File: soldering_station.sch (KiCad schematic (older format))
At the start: 21 parts

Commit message: Change atmega48 to atmega8a
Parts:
- removed U?: ATMEGA48A-PU, DIL28, symbol ATMEGA48A-PU
- added IC?: ATMEGA8A-P, DIL28, symbol ATMEGA8A-P
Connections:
- wire segments 49 -> 61
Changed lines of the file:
@@
 	1    0    0    -1
 $EndComp
-$Comp
-L ATMEGA48A-PU U?
-U 0 1 5901F504
-P 5300 3200
-F 0 "U?" H 5350 4567 50  0000 C CNN
-F 1 "ATMEGA48A-PU" H 5350 4476 50  0000 C CNN
-F 2 "DIL28" H 5300 3200 50  0001 C CIN
-F 3 "" H 5300 3200 50  0001 C CNN
-	0    5300 3200
-	1    0    0    -1
-$EndComp
-Wire Wire Line
-	7150 3900 6300 3900
-Wire Wire Line
-	7150 2200 7150 3900
+Wire Wire Line
+	7150 3850 6300 3850
+Wire Wire Line
+	7150 2200 7150 3850
 Wire Wire Line
 	9850 2200 7150 2200
@@
 Connection ~ 8150 1350
 Wire Wire Line
-	6900 1350 7800 1350
+	6900 1350 7750 1350
+Wire Wire Line
+	7750 1350 7800 1350
 Wire Wire Line
 	7750 1550 7750 1350
@@
 	7750 1750 7750 1850
 Wire Wire Line
-	8100 1350 8250 1350
+	8100 1350 8150 1350
+Wire Wire Line
+	8150 1350 8250 1350
 Wire Wire Line
 	8150 850  8150 1350
@@
 	8350 700  8350 650
 Wire Wire Line
-	8500 850  9100 850
+	8500 850  8550 850
+Wire Wire Line
+	8550 850  9100 850
 Wire Wire Line
 	8550 650  8550 850
 Wire Wire Line
-	9100 1200 9100 1500
+	9100 1200 9100 1450
+Wire Wire Line
+	9100 1450 9100 1500
 Wire Wire Line
 	9100 1800 9100 1850
@@
 Connection ~ 9600 1250
 Wire Wire Line
-	9600 1200 9600 1550
+	9600 1200 9600 1250
+Wire Wire Line
+	9600 1250 9600 1550
 Wire Wire Line
 	9600 1850 9600 1750
 Wire Wire Line
-	9550 1250 10450 1250
+	9550 1250 9600 1250
+Wire Wire Line
+	9600 1250 10450 1250
 $Comp
 L GND #PWR?
@@
 Connection ~ 8150 3050
 Wire Wire Line
-	6300 3050 7800 3050
+	6300 3050 7750 3050
+Wire Wire Line
+	7750 3050 7800 3050
 Wire Wire Line
 	7750 3250 7750 3050
@@
 	7750 3450 7750 3550
 Wire Wire Line
-	8100 3050 8250 3050
+	8100 3050 8150 3050
+Wire Wire Line
+	8150 3050 8250 3050
 Wire Wire Line
 	8150 2550 8150 3050
@@
 	8350 2400 8350 2350
 Wire Wire Line
-	8500 2550 9100 2550
+	8500 2550 8550 2550
+Wire Wire Line
+	8550 2550 9100 2550
 Wire Wire Line
 	8550 2350 8550 2550
 Wire Wire Line
-	9100 2900 9100 3200
+	9100 2900 9100 3150
+Wire Wire Line
+	9100 3150 9100 3200
 Wire Wire Line
 	9100 3500 9100 3550
@@
 Connection ~ 9600 2950
 Wire Wire Line
-	9600 2900 9600 3250
+	9600 2900 9600 2950
+Wire Wire Line
+	9600 2950 9600 3250
 Wire Wire Line
 	9600 3550 9600 3450
 Wire Wire Line
-	9550 2950 10450 2950
+	9550 2950 9600 2950
+Wire Wire Line
+	9600 2950 10450 2950
 $Comp
 L CONN_01X05 J?
@@
 	1    0    0    -1
 $EndComp
+$Comp
+L ATMEGA8A-P IC?
+U 1 1 5912C25D
+P 5300 3350
+F 0 "IC?" H 5350 5018 50  0000 C CNN
+F 1 "ATMEGA8A-P" H 5350 4927 50  0000 C CNN
+F 2 "DIL28" H 5350 4836 50  0000 C CIN
+F 3 "" H 5300 3350 50  0000 C CNN
+	1    5300 3350
+	1    0    0    -1
+$EndComp

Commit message: Add encoder
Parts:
- added BZ?: Buzzer, symbol Buzzer
- added R?: R, symbol R
- added SW?: Rotary_Encoder, symbol Rotary_Encoder
- J?: value CONN_01X05 -> soldering iron
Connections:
- wire segments 61 -> 64
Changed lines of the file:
@@
 U 1 1 5901D04C
 P 8550 1350
-F 0 "U?" H 8600 1050 50  0000 L CNN
-F 1 "TL072" H 8550 1150 50  0000 L CNN
+F 0 "U?" H 8650 1650 50  0000 L CNN
+F 1 "TL072" H 8600 1550 50  0000 L CNN
 F 2 "" H 8550 1350 50  0001 C CNN
 F 3 "" H 8550 1350 50  0001 C CNN
@@
 U 2 1 5901D0A9
 P 8550 3050
-F 0 "U?" H 8891 3096 50  0000 L CNN
-F 1 "TL072" H 8891 3005 50  0000 L CNN
+F 0 "U?" H 8650 3350 50  0000 L CNN
+F 1 "TL072" H 8600 3250 50  0000 L CNN
 F 2 "" H 8550 3050 50  0001 C CNN
 F 3 "" H 8550 3050 50  0001 C CNN
@@
 U 0 1 5901D157
 P 10650 1600
-F 0 "J?" H 10569 1025 50  0000 C CNN
-F 1 "CONN_01X08" H 10569 1116 50  0000 C CNN
+F 0 "J?" H 10600 2200 50  0000 C CNN
+F 1 "CONN_01X08" H 10700 2100 50  0000 C CNN
 F 2 "" H 10650 1600 50  0001 C CNN
 F 3 "" H 10650 1600 50  0001 C CNN
@@
 P 9600 1850
 F 0 "#PWR?" H 9600 1600 50  0001 C CNN
-F 1 "GND" H 9605 1677 50  0000 C CNN
+F 1 "GND" H 9750 1800 50  0000 C CNN
 F 2 "" H 9600 1850 50  0001 C CNN
 F 3 "" H 9600 1850 50  0001 C CNN
@@
 P 9600 750
 F 0 "#PWR?" H 9600 600 50  0001 C CNN
-F 1 "+5V" H 9615 923 50  0000 C CNN
+F 1 "+5V" H 9750 850 50  0000 C CNN
 F 2 "" H 9600 750 50  0001 C CNN
 F 3 "" H 9600 750 50  0001 C CNN
@@
 P 9100 1850
 F 0 "#PWR?" H 9100 1600 50  0001 C CNN
-F 1 "GND" H 9105 1677 50  0000 C CNN
+F 1 "GND" H 9250 1800 50  0000 C CNN
 F 2 "" H 9100 1850 50  0001 C CNN
 F 3 "" H 9100 1850 50  0001 C CNN
@@
 P 7750 1850
 F 0 "#PWR?" H 7750 1600 50  0001 C CNN
-F 1 "GND" H 7755 1677 50  0000 C CNN
+F 1 "GND" H 7900 1800 50  0000 C CNN
 F 2 "" H 7750 1850 50  0001 C CNN
 F 3 "" H 7750 1850 50  0001 C CNN
@@
 P 8650 750
 F 0 "#PWR?" H 8650 600 50  0001 C CNN
-F 1 "+5V" H 8665 923 50  0000 C CNN
+F 1 "+5V" H 8800 850 50  0000 C CNN
 F 2 "" H 8650 750 50  0001 C CNN
 F 3 "" H 8650 750 50  0001 C CNN
@@
 P 8650 1850
 F 0 "#PWR?" H 8650 1600 50  0001 C CNN
-F 1 "GND" H 8655 1677 50  0000 C CNN
+F 1 "GND" H 8800 1800 50  0000 C CNN
 F 2 "" H 8650 1850 50  0001 C CNN
 F 3 "" H 8650 1850 50  0001 C CNN
@@
 $EndComp
 Wire Wire Line
-	7150 3850 6300 3850
-Wire Wire Line
-	7150 2200 7150 3850
-Wire Wire Line
-	9850 2200 7150 2200
+	7200 2200 7200 3150
+Wire Wire Line
+	9850 2200 7200 2200
 Wire Wire Line
 	9850 1350 9850 2200
@@
 Connection ~ 8150 1350
 Wire Wire Line
-	6900 1350 7750 1350
-Wire Wire Line
-	7750 1350 7800 1350
+	6900 1350 7800 1350
 Wire Wire Line
 	7750 1550 7750 1350
@@
 	7750 1750 7750 1850
 Wire Wire Line
-	8100 1350 8150 1350
-Wire Wire Line
-	8150 1350 8250 1350
+	8100 1350 8250 1350
 Wire Wire Line
 	8150 850  8150 1350
@@
 	8350 700  8350 650
 Wire Wire Line
-	8500 850  8550 850
-Wire Wire Line
-	8550 850  9100 850
+	8500 850  9100 850
 Wire Wire Line
 	8550 650  8550 850
 Wire Wire Line
-	9100 1200 9100 1450
-Wire Wire Line
-	9100 1450 9100 1500
+	9100 1200 9100 1500
 Wire Wire Line
 	9100 1800 9100 1850
@@
 Connection ~ 9600 1250
 Wire Wire Line
-	9600 1200 9600 1250
-Wire Wire Line
-	9600 1250 9600 1550
+	9600 1200 9600 1550
 Wire Wire Line
 	9600 1850 9600 1750
 Wire Wire Line
-	9550 1250 9600 1250
-Wire Wire Line
-	9600 1250 10450 1250
+	9550 1250 10450 1250
 $Comp
 L GND #PWR?
@@
 P 9600 3550
 F 0 "#PWR?" H 9600 3300 50  0001 C CNN
-F 1 "GND" H 9605 3377 50  0000 C CNN
+F 1 "GND" H 9750 3500 50  0000 C CNN
 F 2 "" H 9600 3550 50  0001 C CNN
 F 3 "" H 9600 3550 50  0001 C CNN
@@
 P 9600 2450
 F 0 "#PWR?" H 9600 2300 50  0001 C CNN
-F 1 "+5V" H 9615 2623 50  0000 C CNN
+F 1 "+5V" H 9750 2550 50  0000 C CNN
 F 2 "" H 9600 2450 50  0001 C CNN
 F 3 "" H 9600 2450 50  0001 C CNN
@@
 P 9100 3550
 F 0 "#PWR?" H 9100 3300 50  0001 C CNN
-F 1 "GND" H 9105 3377 50  0000 C CNN
+F 1 "GND" H 9250 3500 50  0000 C CNN
 F 2 "" H 9100 3550 50  0001 C CNN
 F 3 "" H 9100 3550 50  0001 C CNN
@@
 P 8650 2450
 F 0 "#PWR?" H 8650 2300 50  0001 C CNN
-F 1 "+5V" H 8665 2623 50  0000 C CNN
+F 1 "+5V" H 8800 2550 50  0000 C CNN
 F 2 "" H 8650 2450 50  0001 C CNN
 F 3 "" H 8650 2450 50  0001 C CNN
@@
 P 8650 3550
 F 0 "#PWR?" H 8650 3300 50  0001 C CNN
-F 1 "GND" H 8655 3377 50  0000 C CNN
+F 1 "GND" H 8800 3500 50  0000 C CNN
 F 2 "" H 8650 3550 50  0001 C CNN
 F 3 "" H 8650 3550 50  0001 C CNN
@@
 Connection ~ 8150 3050
 Wire Wire Line
-	6300 3050 7750 3050
-Wire Wire Line
-	7750 3050 7800 3050
+	6300 3050 7800 3050
 Wire Wire Line
 	7750 3250 7750 3050
@@
 	7750 3450 7750 3550
 Wire Wire Line
-	8100 3050 8150 3050
-Wire Wire Line
-	8150 3050 8250 3050
+	8100 3050 8250 3050
 Wire Wire Line
 	8150 2550 8150 3050
@@
 	8350 2400 8350 2350
 Wire Wire Line
-	8500 2550 8550 2550
-Wire Wire Line
-	8550 2550 9100 2550
+	8500 2550 9100 2550
 Wire Wire Line
 	8550 2350 8550 2550
 Wire Wire Line
-	9100 2900 9100 3150
-Wire Wire Line
-	9100 3150 9100 3200
+	9100 2900 9100 3200
 Wire Wire Line
 	9100 3500 9100 3550
@@
 Connection ~ 9600 2950
 Wire Wire Line
-	9600 2900 9600 2950
-Wire Wire Line
-	9600 2950 9600 3250
+	9600 2900 9600 3250
 Wire Wire Line
 	9600 3550 9600 3450
 Wire Wire Line
-	9550 2950 9600 2950
-Wire Wire Line
-	9600 2950 10450 2950
+	9550 2950 10450 2950
 $Comp
 L CONN_01X05 J?
 U 0 1 59021679
 P 10650 3150
-F 0 "J?" H 10728 3191 50  0000 L CNN
-F 1 "CONN_01X05" H 10728 3100 50  0000 L CNN
+F 0 "J?" H 10550 3600 50  0000 L CNN
+F 1 "soldering iron" H 10500 3500 50  0000 L CNN
 F 2 "" H 10650 3150 50  0001 C CNN
 F 3 "" H 10650 3150 50  0001 C CNN
@@
 	1    0    0    -1
 $EndComp
+$Comp
+L GND #PWR?
+U 1 1 5912E7A7
+P 10000 1500
+F 0 "#PWR?" H 10000 1250 50  0001 C CNN
+F 1 "GND" H 10005 1327 50  0000 C CNN
+F 2 "" H 10000 1500 50  0000 C CNN
+F 3 "" H 10000 1500 50  0000 C CNN
+	1    10000 1500
+	1    0    0    -1
+$EndComp
+Wire Wire Line
+	10450 1450 10000 1450
+Wire Wire Line
+	10000 1450 10000 1500
+$Comp
+L Buzzer BZ?
+U 1 1 5913130E
+P 6800 4450
+F 0 "BZ?" H 6953 4479 50  0000 L CNN
+F 1 "Buzzer" H 6953 4388 50  0000 L CNN
+F 2 "" V 6775 4550 50  0000 C CNN
+F 3 "" V 6775 4550 50  0000 C CNN
+	1    6800 4450
+	1    0    0    -1
+$EndComp
+Wire Wire Line
+	7200 3150 6300 3150
+$Comp
+L GND #PWR?
+U 1 1 59131E18
+P 6400 4650
+F 0 "#PWR?" H 6400 4400 50  0001 C CNN
+F 1 "GND" H 6405 4477 50  0000 C CNN
+F 2 "" H 6400 4650 50  0000 C CNN
+F 3 "" H 6400 4650 50  0000 C CNN
+	1    6400 4650
+	1    0    0    -1
+$EndComp
+Wire Wire Line
+	6700 4550 6400 4550
+Wire Wire Line
+	6400 4550 6400 4650
+$Comp
+L R R?
+U 1 1 59131FE4
+P 6500 4350
+F 0 "R?" V 6293 4350 50  0000 C CNN
+F 1 "R" V 6384 4350 50  0000 C CNN
+F 2 "" V 6430 4350 50  0000 C CNN
+F 3 "" H 6500 4350 50  0000 C CNN
+	1    6500 4350
+	0    1    1    0
+$EndComp
+Wire Wire Line
+	6650 4350 6700 4350
+Wire Wire Line
+	6350 4350 6300 4350
+$Comp
+L Rotary_Encoder SW?
+U 1 1 59133B57
+P 7000 3450
+F 0 "SW?" H 7229 3496 50  0000 L CNN
+F 1 "Rotary_Encoder" H 7229 3405 50  0000 L CNN
+F 2 "" H 6900 3610 50  0001 C CNN
+F 3 "" H 7000 3710 50  0001 C CNN
+	1    7000 3450
+	1    0    0    -1
+$EndComp
+Wire Wire Line
+	6300 3250 6600 3250
+Wire Wire Line
+	6600 3250 6600 3350
+Wire Wire Line
+	6600 3350 6700 3350
+Wire Wire Line
+	6700 3450 6500 3450
+Wire Wire Line
+	6500 3450 6500 3350
+Wire Wire Line
+	6500 3350 6300 3350
+Wire Wire Line
+	6300 3450 6400 3450
+Wire Wire Line
+	6400 3450 6400 3550
+Wire Wire Line
+	6400 3550 6700 3550
 $EndSCHEMATC

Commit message: Add new libs and power regulator
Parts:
- removed J?: soldering iron, symbol CONN_01X05
- added D? (x2): 1N4007, symbol D
- added D? (x2): LED, symbol LED
- added P? (x4): CONN_01X02, symbol CONN_01X02
- added R? (x4): R, symbol R
- added SB?: Switch, symbol Switch
- added SW?: Mode, symbol SW_PUSH
- added U? (x2): MOC3023M, DIP-6, symbol MOC3023M
- added VD? (x2): BT139, symbol BT139
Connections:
- wire segments 64 -> 112
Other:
- moved on the sheet: BZ?, C?, IC?, J?, R?, RV?, SW?, U?A, U?B

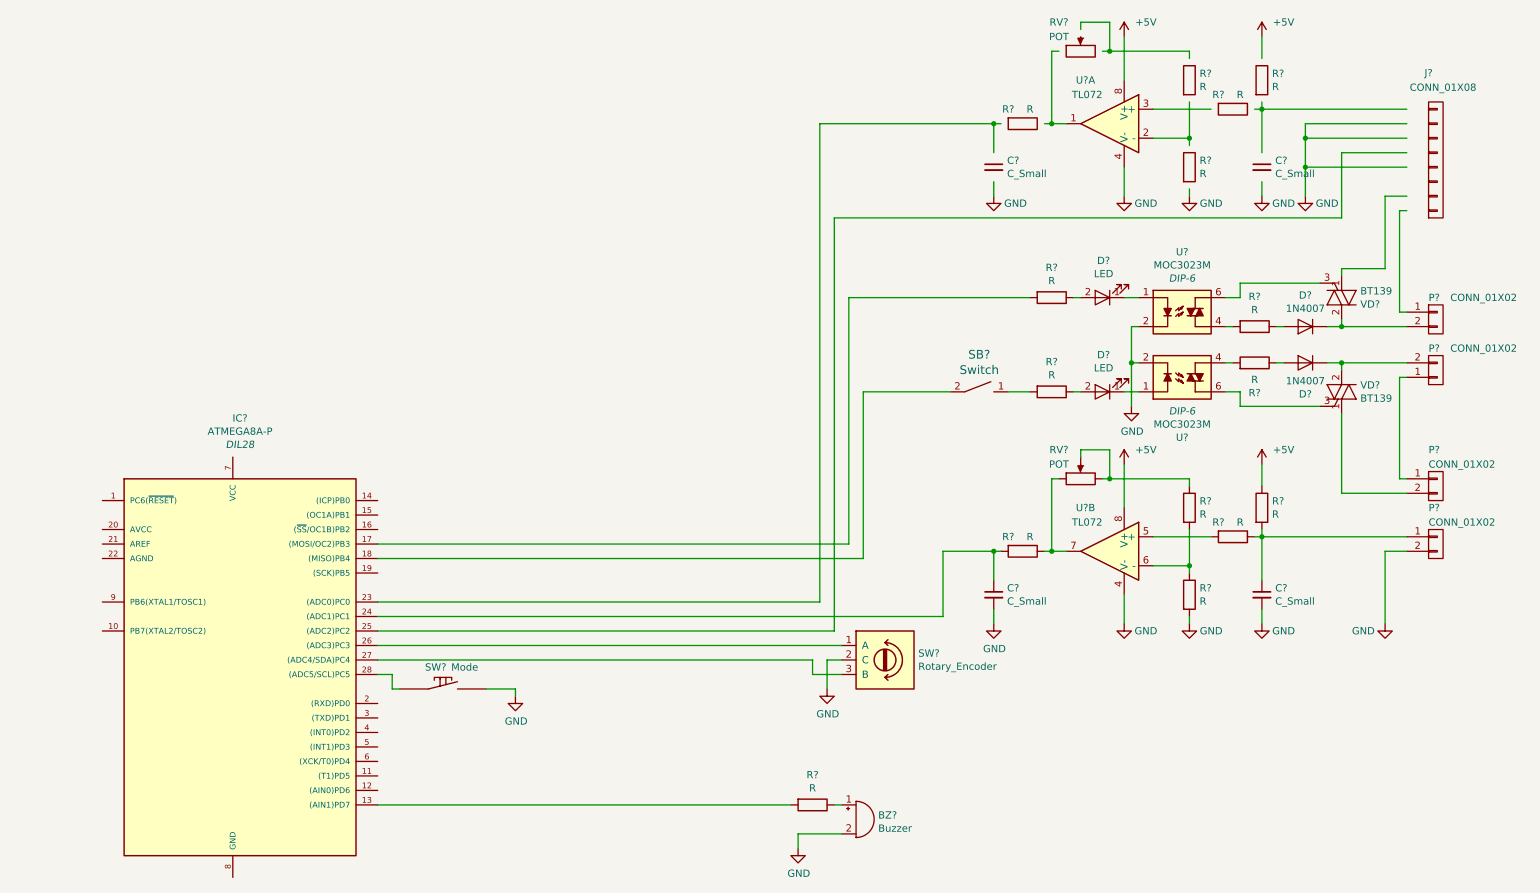
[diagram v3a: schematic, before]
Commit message: Add fan driver
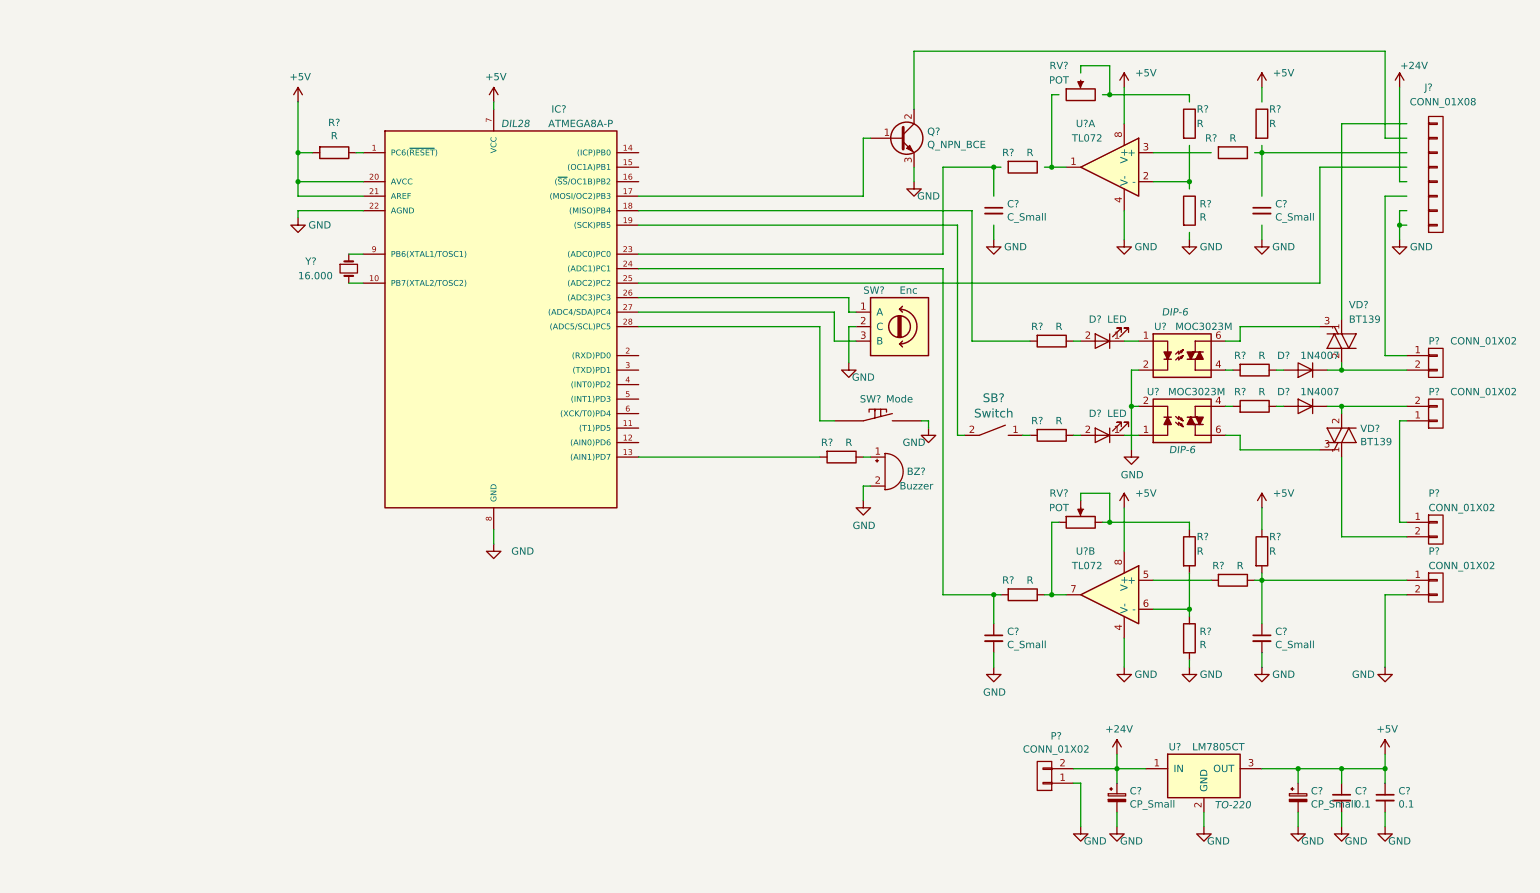
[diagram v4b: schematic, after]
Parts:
- added C? (x2): CP_Small, symbol CP_Small
- added C? (x2): 0.1, symbol C_Small
- added P?: CONN_01X02, symbol CONN_01X02
- added Q?: Q_NPN_BCE, symbol Q_NPN_BCE
- added R?: R, symbol R
- added U?: LM7805CT, TO-220, symbol LM7805CT
- added Y?: 16.000, symbol Crystal_Small
- SW?: value Rotary_Encoder -> Enc
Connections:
- net labels added: +24V
- wire segments 112 -> 166
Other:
- moved on the sheet: BZ?, C?, D?, IC?, J?, P?, R?, RV?, SB?, SW?, U?, U?A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
